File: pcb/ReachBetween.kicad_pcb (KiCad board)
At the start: 2 copper layers, 51.8 x 73.5 mm, 11 parts, among them J1 IN, J2 Out A, J3 Out B

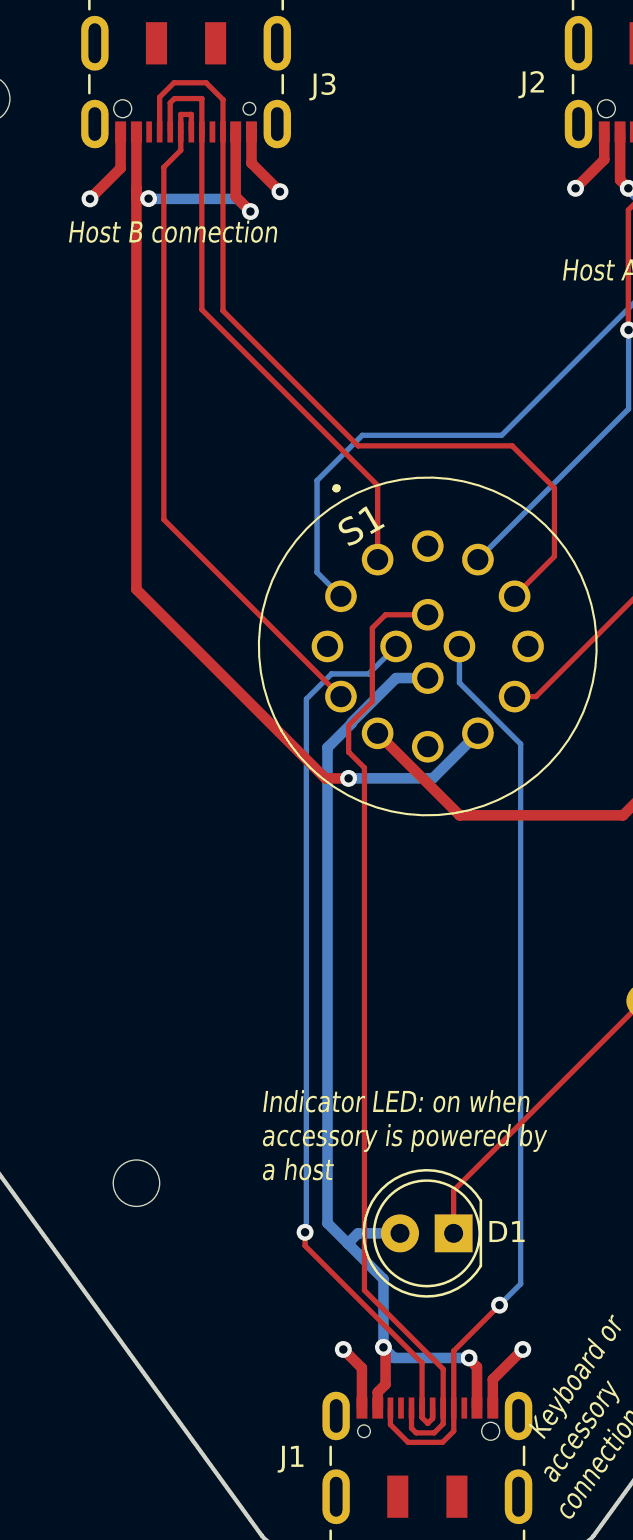
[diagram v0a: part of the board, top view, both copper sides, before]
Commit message: Fix warnings (unconnected tracks)!
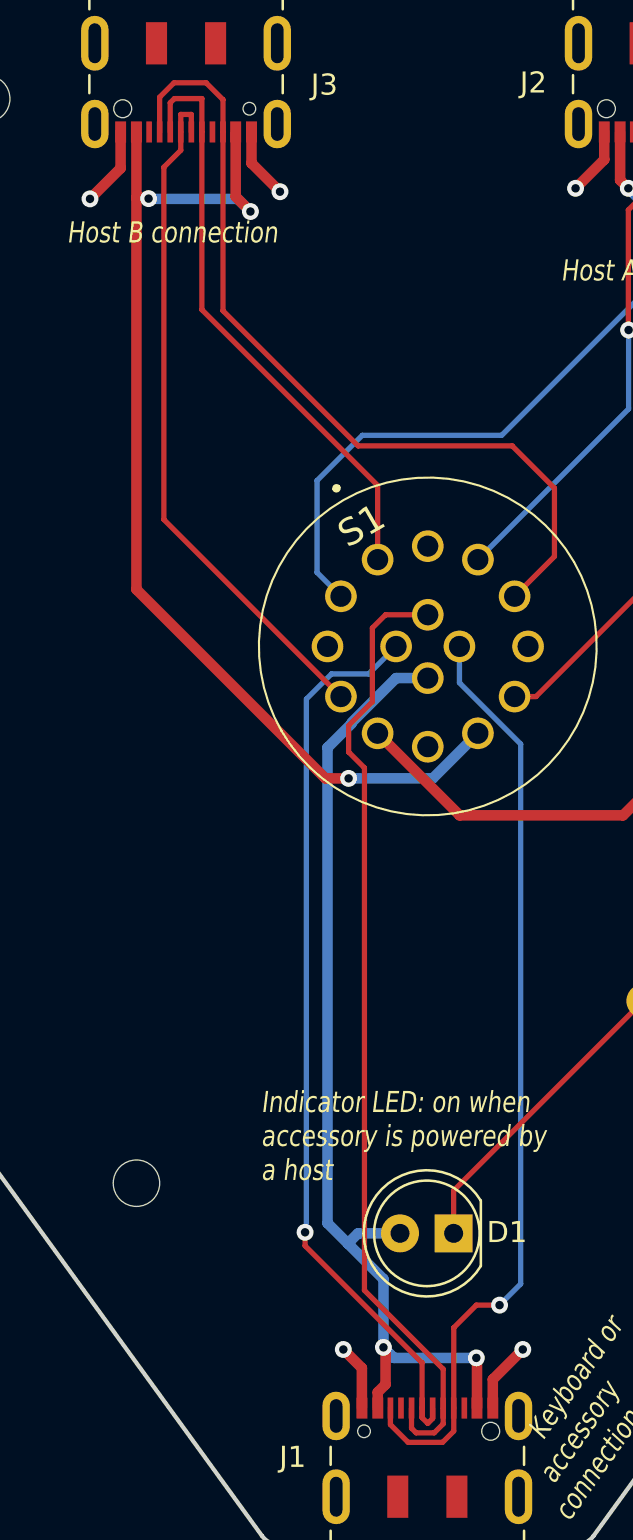
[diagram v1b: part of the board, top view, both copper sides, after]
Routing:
- net /VBUS B: track 53.2 -> 52.2 mm
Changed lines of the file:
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@@
   (segment (start 160.95 73.95) (end 159.5 72.5) (width 0.5) (layer "B.Cu") (net 2))
   (segment (start 163.75 73.95) (end 160.95 73.95) (width 0.5) (layer "B.Cu") (net 2))
-  (segment (start 152.823031 97.865969) (end 152.375 98.314) (width 0.25) (layer "F.Cu") (net 3))
+  (segment (start 145.15 100.45) (end 136.2 91.5) (width 0.5) (layer "F.Cu") (net 3))
   (segment (start 140.9 72.9) (end 140.9 69.83) (width 0.5) (layer "F.Cu") (net 3))
+  (segment (start 136.2 91.5) (end 136.2 69.83) (width 0.5) (layer "F.Cu") (net 3))
   (segment (start 136.2 72.95) (end 136.737799 72.95) (width 0.5) (layer "F.Cu") (net 3))
   (segment (start 136.737799 72.95) (end 136.7755 72.987701) (width 0.5) (layer "F.Cu") (net 3))
-  (segment (start 136.2 72.95) (end 136.2 72.5) (width 0.5) (layer "F.Cu") (net 3))
   (segment (start 140.9 72.9) (end 141.6 73.6) (width 0.5) (layer "F.Cu") (net 3))
-  (segment (start 136.2 91.5) (end 136.2 72.5) (width 0.5) (layer "F.Cu") (net 3))
   (segment (start 146.25 100.45) (end 145.15 100.45) (width 0.5) (layer "F.Cu") (net 3))
-  (segment (start 136.2 72.5) (end 136.2 69.83) (width 0.5) (layer "F.Cu") (net 3))
-  (segment (start 145.15 100.45) (end 136.2 91.5) (width 0.5) (layer "F.Cu") (net 3))
   (via (at 146.25 100.45) (size 0.8) (drill 0.4) (layers "F.Cu" "B.Cu") (net 3))
   (via (at 136.7755 72.987701) (size 0.8) (drill 0.4) (layers "F.Cu" "B.Cu") (net 3))
@@
   (segment (start 147.9 127.4) (end 148 127.5) (width 0.5) (layer "F.Cu") (net 5))
   (segment (start 147.63 129.525) (end 147.63 130.275) (width 0.5) (layer "F.Cu") (net 5))
-  (segment (start 151.9545 127.9) (end 151.9545 127.9545) (width 0.5) (layer "F.Cu") (net 5))
+  (segment (start 152.33 127.93) (end 152.33 130.275) (width 0.5) (layer "F.Cu") (net 5))
   (segment (start 148 129.155) (end 147.63 129.525) (width 0.5) (layer "F.Cu") (net 5))
   (segment (start 148 127.5) (end 148 129.155) (width 0.5) (layer "F.Cu") (net 5))
-  (segment (start 152.33 128.33) (end 152.33 130.275) (width 0.5) (layer "F.Cu") (net 5))
-  (segment (start 151.9545 127.9545) (end 152.33 128.33) (width 0.5) (layer "F.Cu") (net 5))
   (via (at 147.9 127.4) (size 0.8) (drill 0.4) (layers "F.Cu" "B.Cu") (net 5))
-  (via (at 151.9545 127.9) (size 0.8) (drill 0.4) (layers "F.Cu" "B.Cu") (net 5))
+  (via (at 152.3 127.9) (size 0.8) (drill 0.4) (layers "F.Cu" "B.Cu") (net 5))
   (segment (start 146.7 122) (end 146.217736 122.482264) (width 0.5) (layer "B.Cu") (net 5))
   (segment (start 148.685 122) (end 146.7 122) (width 0.5) (layer "B.Cu") (net 5))
   (segment (start 148.500033 95.699967) (end 146.4 97.8) (width 0.5) (layer "B.Cu") (net 5))
   (segment (start 145.25 98.992634) (end 145.25 121.514528) (width 0.5) (layer "B.Cu") (net 5))
-  (segment (start 151.9545 127.9) (end 148.4 127.9) (width 0.5) (layer "B.Cu") (net 5))
+  (segment (start 148.4 127.9) (end 147.9 127.4) (width 0.5) (layer "B.Cu") (net 5))
   (segment (start 147.9 124.164528) (end 147.9 127.4) (width 0.5) (layer "B.Cu") (net 5))
   (segment (start 146.217736 122.482264) (end 147.9 124.164528) (width 0.5) (layer "B.Cu") (net 5))
   (segment (start 146.4 97.842634) (end 145.25 98.992634) (width 0.5) (layer "B.Cu") (net 5))
-  (segment (start 148.4 127.9) (end 147.9 127.4) (width 0.5) (layer "B.Cu") (net 5))
   (segment (start 149.999981 95.699967) (end 148.500033 95.699967) (width 0.5) (layer "B.Cu") (net 5))
+  (segment (start 152.3 127.9) (end 148.4 127.9) (width 0.5) (layer "B.Cu") (net 5))
   (segment (start 145.25 121.514528) (end 146.217736 122.482264) (width 0.5) (layer "B.Cu") (net 5))
-  (segment (start 153.4 125.4) (end 151.23 127.57) (width 0.25) (layer "F.Cu") (net 6))
+  (segment (start 152.3 125.4) (end 151.23 126.47) (width 0.25) (layer "F.Cu") (net 6))
   (segment (start 148.23 131.059022) (end 149.070018 131.89904) (width 0.25) (layer "F.Cu") (net 6))
   (segment (start 151.23 131.369511) (end 151.23 130.275) (width 0.25) (layer "F.Cu") (net 6))
-  (segment (start 151.23 127.57) (end 151.23 130.275) (width 0.25) (layer "F.Cu") (net 6))
   (segment (start 149.070018 131.89904) (end 150.700471 131.89904) (width 0.25) (layer "F.Cu") (net 6))
   (segment (start 148.23 130.275) (end 148.23 131.059022) (width 0.25) (layer "F.Cu") (net 6))
+  (segment (start 153.4 125.4) (end 152.3 125.4) (width 0.25) (layer "F.Cu") (net 6))
+  (segment (start 151.23 126.47) (end 151.23 130.275) (width 0.25) (layer "F.Cu") (net 6))
   (segment (start 150.700471 131.89904) (end 151.23 131.369511) (width 0.25) (layer "F.Cu") (net 6))
   (via (at 153.4 125.4) (size 0.8) (drill 0.4) (layers "F.Cu" "B.Cu") (net 6))
+  (segment (start 154.4 98.819032) (end 151.499967 95.918999) (width 0.25) (layer "B.Cu") (net 6))
+  (segment (start 154.4 124.4) (end 154.4 98.819032) (width 0.25) (layer "B.Cu") (net 6))
   (segment (start 153.4 125.4) (end 154.4 124.4) (width 0.25) (layer "B.Cu") (net 6))
   (segment (start 151.499967 95.918999) (end 151.499967 94.200019) (width 0.25) (layer "B.Cu") (net 6))
-  (segment (start 154.4 98.819032) (end 151.499967 95.918999) (width 0.25) (layer "B.Cu") (net 6))
-  (segment (start 151.299 94.400986) (end 151.499967 94.200019) (width 0.25) (layer "B.Cu") (net 6))
-  (segment (start 154.4 124.4) (end 154.4 98.819032) (width 0.25) (layer "B.Cu") (net 6))
   (segment (start 150 131) (end 150.23 130.77) (width 0.25) (layer "F.Cu") (net 8))
   (segment (start 149.73 130.73) (end 150 131) (width 0.25) (layer "F.Cu") (net 8))
